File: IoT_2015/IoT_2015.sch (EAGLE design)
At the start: 29 parts, among them Y1 ABLS-16.000MHZ-B4-T

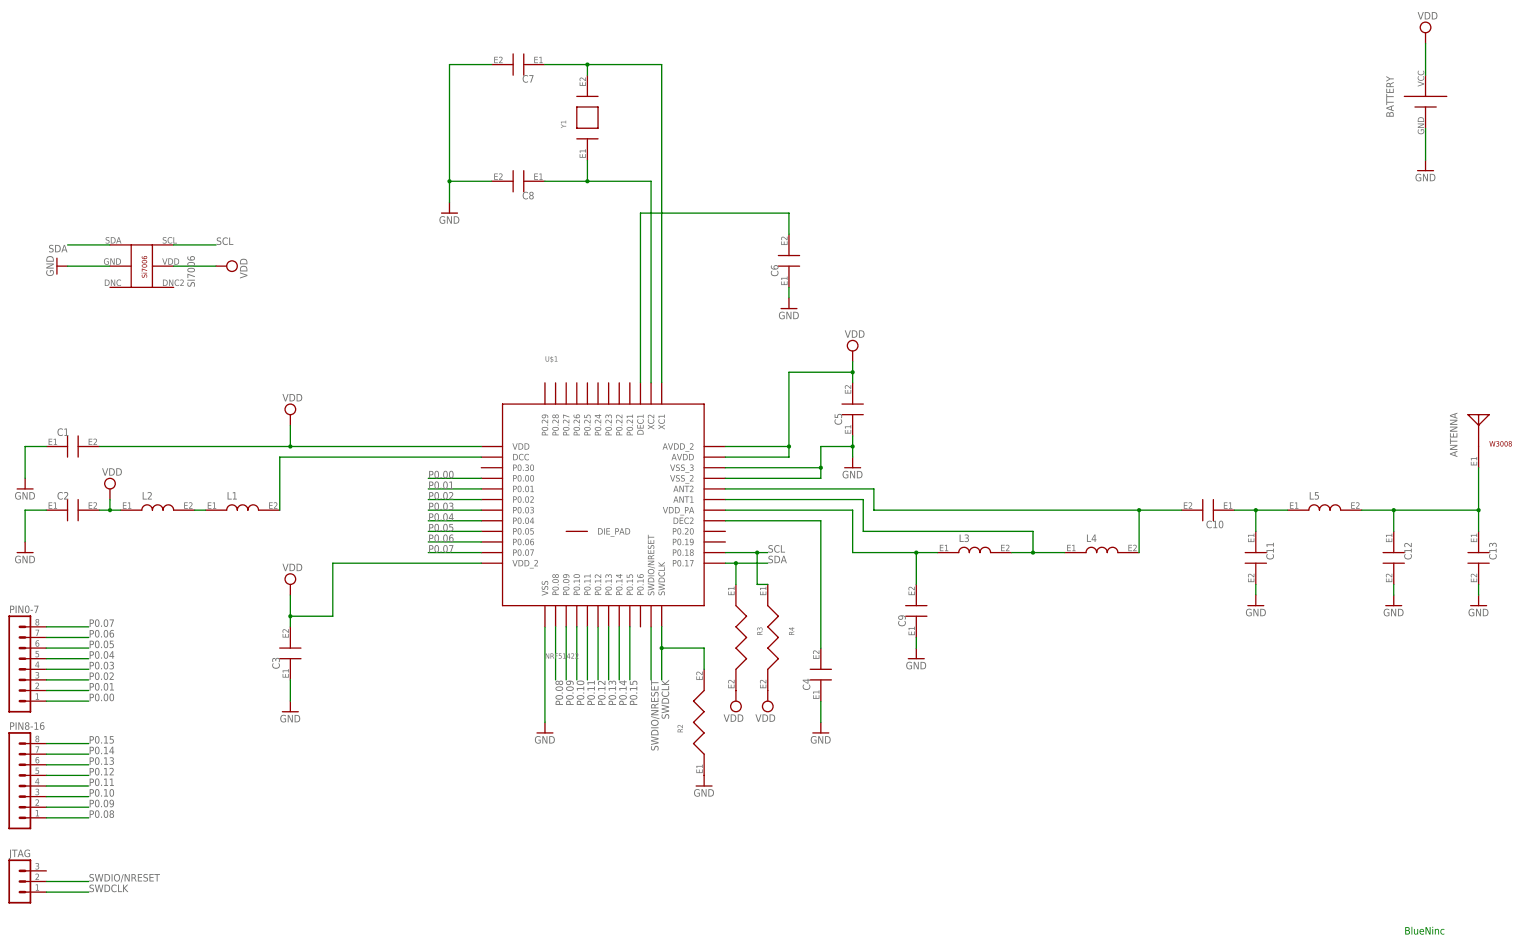
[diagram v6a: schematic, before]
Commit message: Refining
Changed the battery holder, deleted some pinheaders
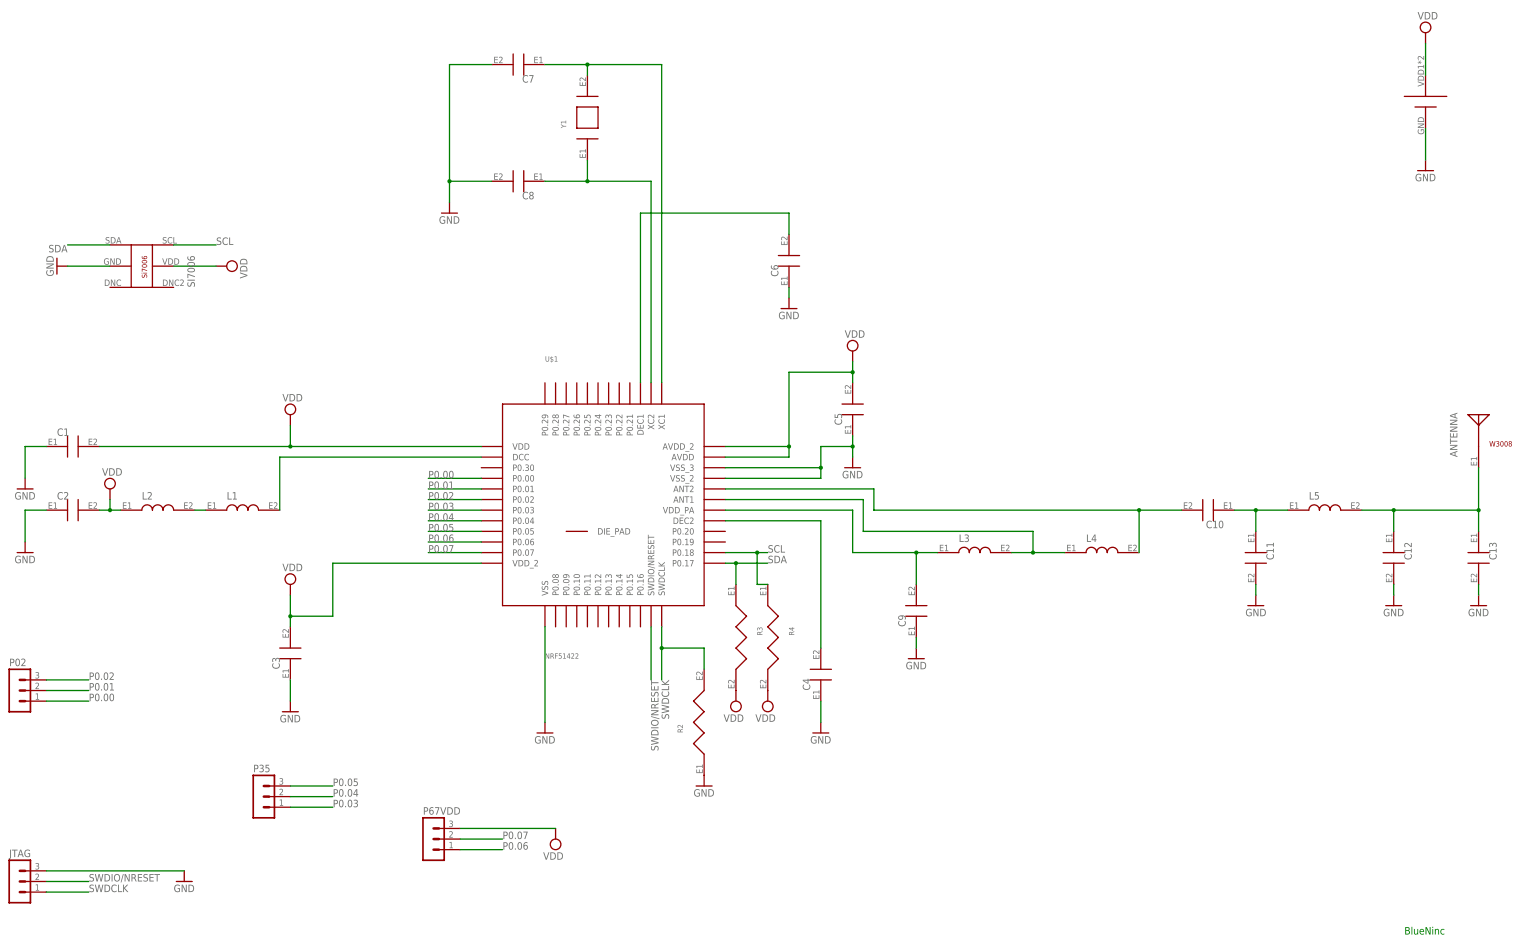
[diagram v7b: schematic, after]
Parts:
- removed PIN0-7, PIN8-16: (no value), con-lstb:MA08-1
- added P02, P35, P67VDD: (no value), con-lstb:MA03-1
- BATTERY: value SMTU2032-G.TR -> BAT-HLD-001; device Renata:SMTU2032-G.TR -> BAT-HLD-001:BAT-HLD-001
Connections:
- removed net P0.08: PIN8-16.1, U$1.P0.08
- removed net P0.09: PIN8-16.2, U$1.P0.09
- removed net P0.10: PIN8-16.3, U$1.P0.10
- removed net P0.11: PIN8-16.4, U$1.P0.11
- removed net P0.12: PIN8-16.5, U$1.P0.12
- removed net P0.13: PIN8-16.6, U$1.P0.13
- removed net P0.14: PIN8-16.7, U$1.P0.14
- removed net P0.15: PIN8-16.8, U$1.P0.15
- net GND: now also JTAG.3
- net P0.00: now also P02.1; no longer PIN0-7.1
- net P0.01: now also P02.2; no longer PIN0-7.2
- net P0.02: now also P02.3; no longer PIN0-7.3
- net P0.03: now also P35.1; no longer PIN0-7.4
- net P0.04: now also P35.2; no longer PIN0-7.5
- net P0.05: now also P35.3; no longer PIN0-7.6
- net P0.06: now also P67VDD.1; no longer PIN0-7.7
- net P0.07: now also P67VDD.2; no longer PIN0-7.8
- net VDD: now also BATTERY.VDD, P67VDD.3; no longer BATTERY.VCC
